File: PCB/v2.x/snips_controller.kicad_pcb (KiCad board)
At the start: 4 copper layers, 30 x 70 mm, 95 parts

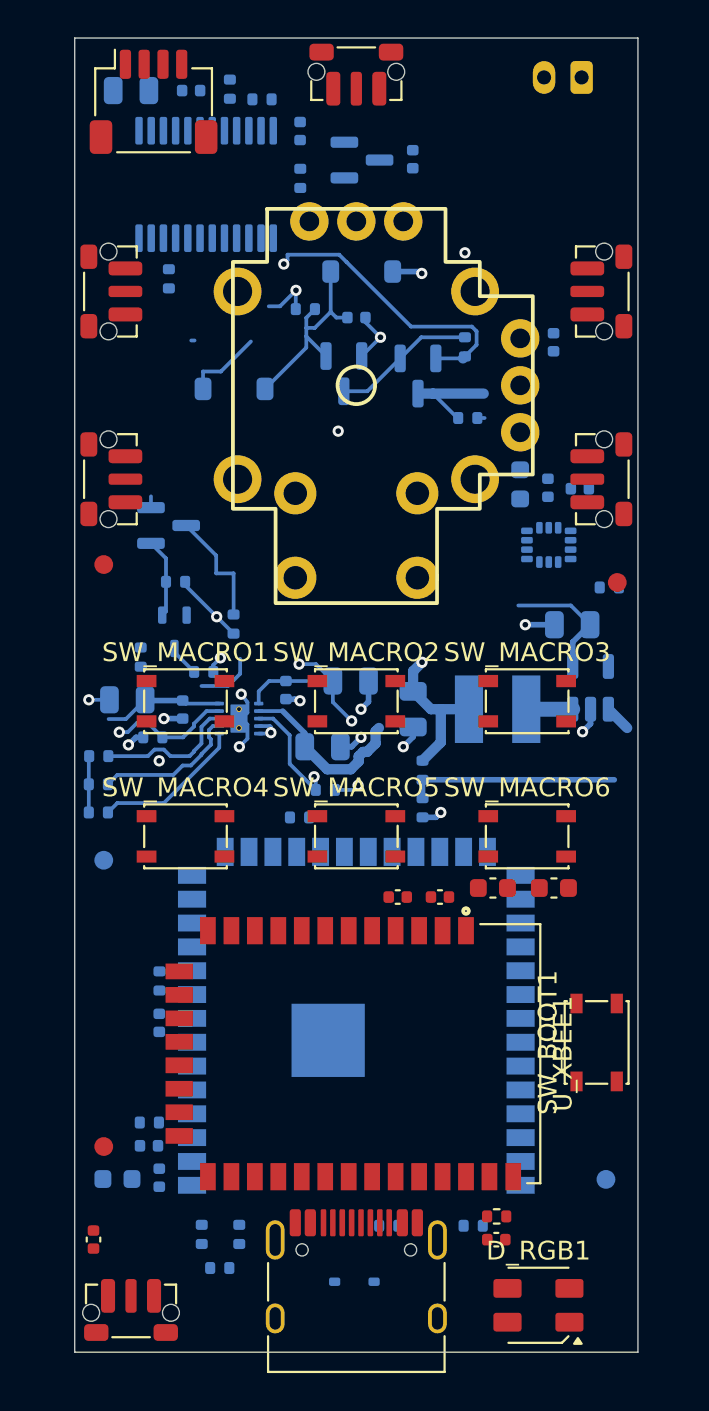
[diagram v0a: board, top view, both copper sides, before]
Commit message: Replace the V2 ESP32 and XBee with a BT840XE module (#97)
The XBee and ESP32 could not sit back to back: Espressif allows one
reflow and Digi forbids reflowing the XBee upside down. A single Fanstel
BT840XE (nRF52840 with PA) now runs the firmware and the Zigbee link.

The module sits on the bottom and reflows last, as Fanstel allows no
opposite-side reflow. The buck and charger moved to the top as rigid
blocks, with V1's copper. U_EXP1 is gone, since the module has enough
GPIOs for direct buttons.

Also from the pre-routing review:
- Hall sensor and stick on 3V3_RF, so they track the ADC reference
- RC filter on the trigger output
- 10 uF on the buck output, as the rail exceeded TI's 47 uF limit
- VBUS bypass at the module
- Tag-Connect SWD pads and a reset button
- Four M2 mounting holes
- Silkscreen reduced to labels a builder needs

Placed, not routed.

Co-authored-by: Claude Opus 5.5 <noreply@anthropic.com>
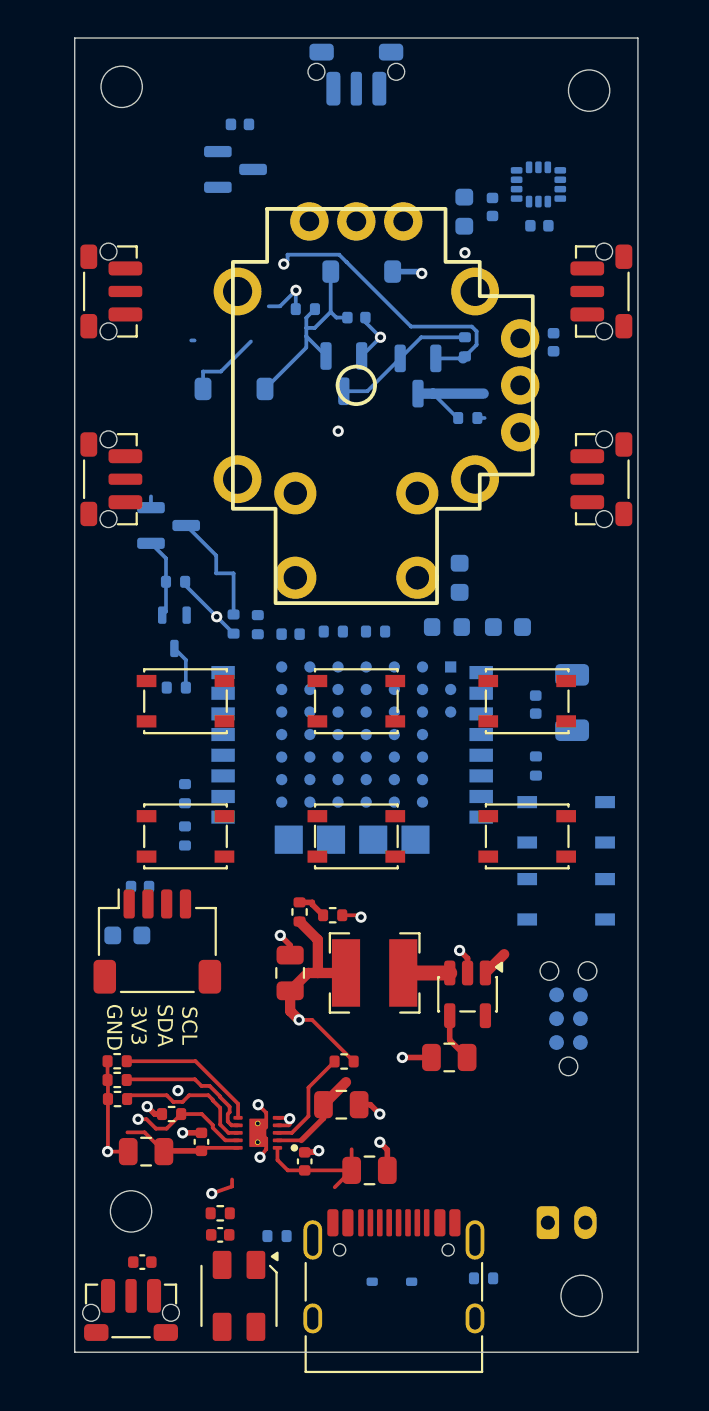
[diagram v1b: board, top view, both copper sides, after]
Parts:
- removed C_3V3_3: 39pF, Capacitor_SMD:C_0402_1005Metric
- removed C_EXP1: 100nF, C_0402_1005Metric
- removed C_XBEE_RC1, C_XBEE_VCC1: 100nF, Capacitor_SMD:C_0402_1005Metric
- removed C_XBEE_VCC2: 1µF, Capacitor_SMD:C_0603_1608Metric
- removed C_XBEE_VCC3: 47pF, Capacitor_SMD:C_0402_1005Metric
- removed C_XBEE_VCC4: 10µF, Capacitor_SMD:C_0603_1608Metric
- removed FID1, FID2, FID3, FID4, FID5: Fiducial_1mm_Mask2mm, Fiducial:Fiducial_1mm_Mask2mm
- removed R_EN_PU1, R_XBEE_ATTN_PU1, R_XBEE_RST1: 10kΩ, Resistor_SMD:R_0402_1005Metric
- removed R_EXP_INT1: 10kΩ, R_0402_1005Metric
- removed R_USB_DM1, R_USB_DP1: 27Ω, Resistor_SMD:R_0402_1005Metric
- removed R_XBEE_RC1: 100Ω, Resistor_SMD:R_0402_1005Metric
- removed U_EXP1: TCA9555PWR, TSSOP-24_4.4x7.8mm_P0.65mm
- removed U_XBEE1: XBee3 PRO Micro, XB3-24Z8UM
- added C_RF_BULK1: 47µF, C_1206_3216Metric, B.Cu at (146.5, 95.4)
- added C_TRIG1: 100nF, C_0402_1005Metric, B.Cu at (131.5, 91.8)
- added C_VBUS1: 1µF, C_0603_1608Metric, B.Cu at (140.5, 88.8)
- added FB_RF1: 600Ω@100MHz, L_0603_1608Metric, B.Cu at (139.8, 91.4)
- added J_SWD1: TC2030-NL, Tag-Connect_TC2030-IDC-NL_2x03_P1.27mm_Vertical, B.Cu at (146.3, 112.2)
- added MH1: MountingHole_2.2mm_M2_ISO14580, MountingHole:MountingHole_2.2mm_M2_ISO14580, F.Cu at (122.5, 62.6)
- added MH2: MountingHole_2.2mm_M2_ISO14580, MountingHole:MountingHole_2.2mm_M2_ISO14580, F.Cu at (147.4, 62.8)
- added MH3: MountingHole_2.2mm_M2_ISO14580, MountingHole:MountingHole_2.2mm_M2_ISO14580, F.Cu at (123.0, 122.5)
- added MH4: MountingHole_2.2mm_M2_ISO14580, MountingHole:MountingHole_2.2mm_M2_ISO14580, F.Cu at (147.0, 127.0)
- added R_TRIG1: 1kΩ, R_0402_1005Metric, B.Cu at (129.8, 91.2)
- added SW_RST1: SKRPABE010, SW_Alps_SKRP, B.Cu at (146.2, 101.8)
- C_BAT1, C_BUCK_IN1, C_SYS_1, C_SYS_2, C_VIN_1, C_VIN_2, L_BUCK1, R_FB1, R_FB2, R_ISET1, R_STAT1, R_STAT2, R_TS1, R_VSET1, U_BUCK1, U_CHG1: moved to F.Cu
- C_BUCK_OUT1: value 22µF -> 10µF; moved to F.Cu
- C_OLED_1: value 10µF -> 1µF; footprint Capacitor_SMD:C_0805_2012Metric -> C_0603_1608Metric
- SW_BOOT1, SW_TRIG_DIG1: moved to B.Cu
- U_MCU1: value ESP32-S3-WROOM-1U-N8 -> BT840XE; footprint ESP32-S3-WROOM-1U -> BT840XE
- moved BT1 61.0 mm to (145.2, 123.1), turned to 0 degrees
- moved C_OLED_1 45.0 mm to (122.8, 107.8), turned to 180 degrees
- moved U_OLED1 44.7 mm to (124.4, 108.1)
- moved C_OLED_2 42.5 mm to (123.5, 105.2), turned to 180 degrees
- moved R_I2C_SDA1 39.4 mm to (125.9, 102.5), turned to 90 degrees
- moved R_I2C_SCL1 37.6 mm to (125.9, 100.2)
- moved C_3V3_1 36.0 mm to (143.1, 91.4)
- moved C_3V3_2 32.2 mm to (144.6, 95.5)
- moved C_SYS_1 26.1 mm to (135.7, 120.3)
- moved C_SYS_2 25.1 mm to (132.2, 119.8), turned to 90 degrees
- moved C_VIN_1 24.1 mm to (123.8, 119.3)
- moved C_BUCK_IN1 24.0 mm to (139.9, 114.3)
- moved C_VIN_2 23.0 mm to (126.8, 118.8), turned to 90 degrees
- moved U_CHG1 22.1 mm to (129.8, 118.3)
- moved R_VSYS1 20.7 mm to (133.8, 91.6), turned to 0 degrees
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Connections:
- C_3V3_1 pad 1: 3V3 -> /MCU_Core/3V3_RF
- C_3V3_2 pad 1: 3V3 -> /MCU_Core/3V3_RF
- C_HALL1 pad 1: 3V3 -> /MCU_Core/3V3_RF
- C_STICK1 pad 1: 3V3 -> /MCU_Core/3V3_RF
- J_STICK1 pad 3: 3V3 -> /MCU_Core/3V3_RF
- J_STICK1 pad 3': 3V3 -> /MCU_Core/3V3_RF
- U_HALL1 pad 1: 3V3 -> /MCU_Core/3V3_RF
- U_MCU1 pad 1: GND -> /Accelerometer/I2C_SDA
- U_MCU1 pad 10: /Buttons_Direct/BTN_THR_DN -> GND
- U_MCU1 pad 11: /Buttons_Direct/BTN_INT -> /MCU_Core/PWR_BTN_SENSE
- U_MCU1 pad 12: /Accelerometer/I2C_SDA -> /MCU_Core/MCU_BOOT
- U_MCU1 pad 13: /MCU_Core/USB_DM_MCU -> /MCU_Core/RGB_DIN
- U_MCU1 pad 14: /MCU_Core/USB_DP_MCU -> /MCU_Core/MCU_RESET
- U_MCU1 pad 15: (no net) -> /MCU_Core/SWDCLK
- U_MCU1 pad 16: ACCEL_INT1 -> /MCU_Core/SWDIO
- U_MCU1 pad 2: 3V3 -> /Accelerometer/I2C_SCL
- U_MCU1 pad 3: /MCU_Core/MCU_EN -> (no net)
- U_MCU1 pad 4: /Hall_Trigger/TRIG_ANALOG -> (no net)
- U_MCU1 pad 7: /MCU_Core/VSYS_SENSE -> (no net)
- U_MCU1 pad 8: /XBee/XBEE_SPI_ATTN -> (no net)
- U_MCU1 pad 9: /Buttons_Direct/BTN_THR_UP -> /MCU_Core/3V3_RF
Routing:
- net /Power_Buck/BUCK_FB: track 11.2 -> 1.60 mm
- net VSYS: track 36.2 -> 29.6 mm, vias 4 -> 2
- net VBAT: track 9.56 -> 5.36 mm
- net 3V3: track 11.5 -> 14.6 mm, vias 4 -> 3
- net /MCU_Core/PWR_BTN_SENSE: track 4.83 -> 2.54 mm
- net GND: track 26.0 -> 27.8 mm
- net /MCU_Core/STAT2: track 6.25 -> 5.51 mm, vias 1 -> 0
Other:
- board text added: "+"
- board text added: "-"
- board text added: "3V3"
- board text added: "BOOT"
- board text added: "GND"
- board text added: "RESET"
- board text added: "SCL"
- board text added: "SDA"

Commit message: Route the V2 board and add production files
Fully routed on four layers: In2 is a solid ground plane, and In1 carries
signals with a partial 3V3 fill. BUCK_FB stays on the top layer and out
from under the inductor. Every GND pad has a via to the plane.

BTN_MACRO4 moved from P0.21 (E2) to P1.11 (Z0), since E2 had no escape
and Z0 sits beside the button.

Adds six fiducials, the Snips logo at 80%, a lower-density QR code that
prints at 5.5 mm, and the V2.0 text. Production files follow V1's layout.

Co-Authored-By: Claude Opus 5.5 <noreply@anthropic.com>
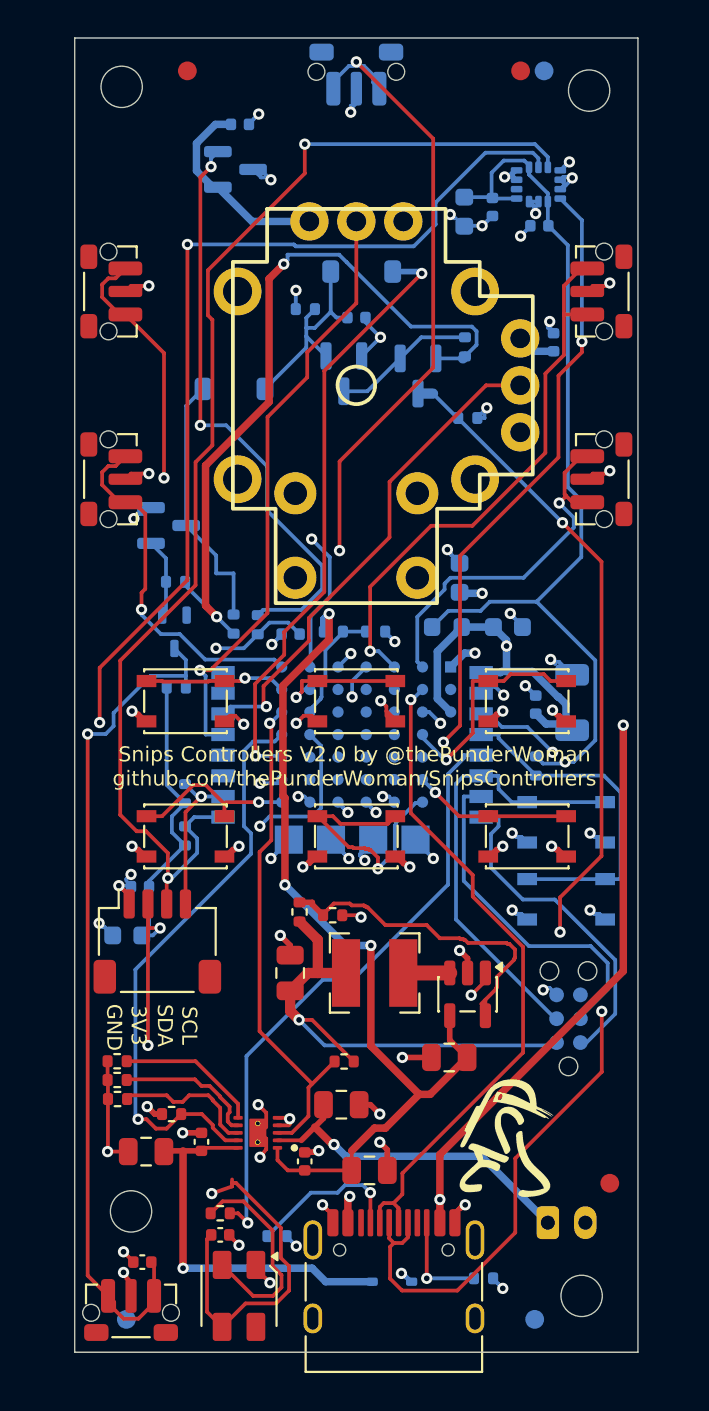
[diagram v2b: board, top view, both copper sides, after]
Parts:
- added FID1: Fiducial_1mm_Mask2mm, Fiducial:Fiducial_1mm_Mask2mm, F.Cu at (126.0, 61.8)
- added FID2: Fiducial_1mm_Mask2mm, Fiducial:Fiducial_1mm_Mask2mm, F.Cu at (143.8, 61.8)
- added FID3: Fiducial_1mm_Mask2mm, Fiducial:Fiducial_1mm_Mask2mm, F.Cu at (148.5, 121.0)
- added FID4: Fiducial_1mm_Mask2mm, Fiducial:Fiducial_1mm_Mask2mm, B.Cu at (145.0, 61.8)
- added FID5: Fiducial_1mm_Mask2mm, Fiducial:Fiducial_1mm_Mask2mm, B.Cu at (122.8, 128.2)
- added FID6: Fiducial_1mm_Mask2mm, Fiducial:Fiducial_1mm_Mask2mm, B.Cu at (144.5, 128.2)
- LOGO3: moved to F.Cu
- moved LOGO2 65.7 mm to (123.1, 115.0)
- moved LOGO3 63.9 mm to (143.0, 118.6), turned to 0 degrees
- moved LOGO1 32.8 mm to (123.2, 67.2), turned to 0 degrees
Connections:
- U_MCU1 pad E2: /Buttons_Direct/BTN_MACRO4 -> (no net)
- U_MCU1 pad Z0: (no net) -> /Buttons_Direct/BTN_MACRO4
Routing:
- net 3V3: track 14.6 -> 163.9 mm, vias 3 -> 6
- net VBUS: track 6.40 -> 85.7 mm, vias 0 -> 6
- net /MCU_Core/PWR_BTN_SENSE: track 2.54 -> 79.3 mm, vias 0 -> 2
- net GND: track 27.8 -> 95.0 mm, vias 16 -> 75
- net /Accelerometer/I2C_SDA: track 0.00 -> 65.9 mm, vias 0 -> 2
- net VSYS: track 29.6 -> 94.8 mm, vias 2 -> 5
- net /Accelerometer/I2C_SCL: track 0.00 -> 64.9 mm, vias 0 -> 3
- net /MCU_Core/3V3_RF: track 0.00 -> 62.9 mm, vias 0 -> 1
- net /MCU_Core/USB_DP: track 0.00 -> 50.3 mm, vias 0 -> 2
- net ACCEL_INT1: track 0.00 -> 44.4 mm, vias 0 -> 3
- net /Buttons_Direct/BTN_TRIG_DIG: track 0.00 -> 43.9 mm, vias 0 -> 3
- net /MCU_Core/USB_DM: track 0.00 -> 35.8 mm, vias 0 -> 1
- net /Power_Buck/PWR_EN: track 6.79 -> 41.8 mm, vias 1 -> 3
- net /MCU_Core/RGB_DIN: track 0.00 -> 32.8 mm, vias 0 -> 1
- net /MCU_Core/STICK_X: track 0.00 -> 32.2 mm, vias 0 -> 1
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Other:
- board text added: "Snips Controllers V2.0 by @thePunderWoman github.com/thePunderWoman/SnipsControllers"

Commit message: V2 PCB: ESP32-S3-MINI-1U with an optional castellated XBee carrier
Replace the BT840XE with an ESP32-S3-MINI-1U-N8 on the top side, and move
the XBee to an optional hand-soldered daughter board on the underside,
linked by UART with flow control instead of SPI. The WROOM-1U does not fit
between the macro row and USB; the MINI-1U does.

Turn the module 270 degrees and assign pins by position, so the signal
pins face the stick, OLED and carrier. PWR_HOLD stays on RXD0, whose
reset pull-up holds the latch, and IO26 stays unconnected because
Arduino's PSRAM probe drives it at every boot.

Put the buck and charger back on the bottom, remove the reset button and
SWD footprint, move the hall sensor away from the stick, reroute the
board, and regenerate the production files.

Co-Authored-By: Claude Opus 5.5 <noreply@anthropic.com>
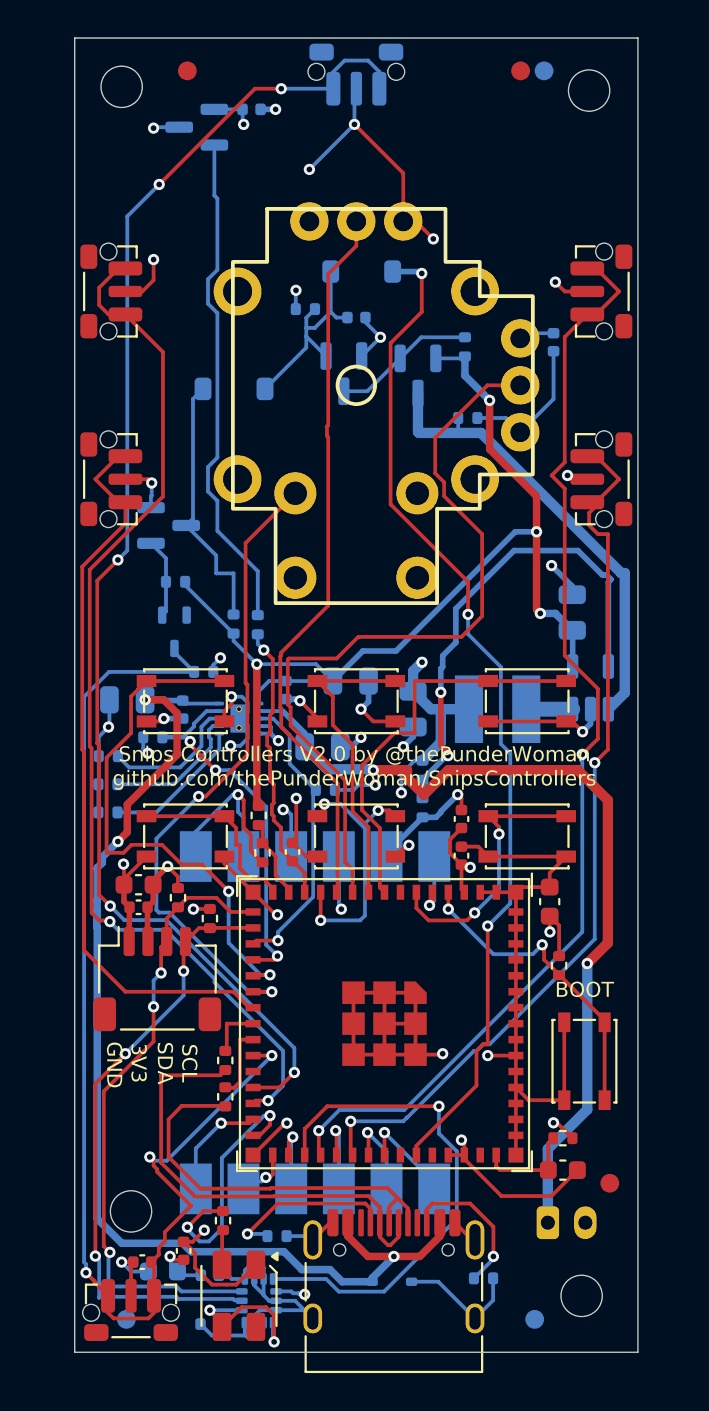
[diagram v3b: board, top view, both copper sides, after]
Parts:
- removed C_RF_BULK1: 47µF, C_1206_3216Metric
- removed C_VBUS1: 1µF, C_0603_1608Metric
- removed FB_RF1: 600Ω@100MHz, L_0603_1608Metric
- removed J_SWD1: TC2030-NL, Tag-Connect_TC2030-IDC-NL_2x03_P1.27mm_Vertical
- removed SW_RST1: SKRPABE010, SW_Alps_SKRP
- added C_3V3_3: 39pF, C_0402_1005Metric, F.Cu at (140.6, 103.5)
- added C_EN1: 1µF, C_0603_1608Metric, F.Cu at (146.0, 120.3)
- added R_EN_PU1: 10kΩ, R_0402_1005Metric, F.Cu at (146.0, 118.6)
- added R_USB_DM1: 27Ω, R_0402_1005Metric, F.Cu at (128.0, 114.5)
- added R_USB_DP1: 27Ω, R_0402_1005Metric, F.Cu at (128.0, 116.4)
- added U_XBEE1: XBee carrier, XBee_Carrier_Castellated, B.Cu at (131.5, 112.5)
- C_3V3_1, C_3V3_2, C_OLED_1, C_OLED_2, C_TRIG1, R_BOOT_PU1, R_I2C_SCL1, R_I2C_SDA1, R_VSYS1, R_VSYS2, SW_BOOT1: moved to F.Cu
- C_BAT1, C_BUCK_IN1, C_SYS_1, C_SYS_2, C_VIN_1, C_VIN_2, LOGO3, L_BUCK1, R_FB1, R_FB2, R_ISET1, R_STAT1, R_STAT2, R_TS1, R_VSET1, U_BUCK1, U_CHG1: moved to B.Cu
- C_BUCK_OUT1: value 10µF -> 22µF; moved to B.Cu
- U_MCU1: value BT840XE -> ESP32-S3-MINI-1U-N8; footprint BT840XE -> ESP32-S3-MINI-1U; moved to F.Cu
- moved U_IMU1 61.3 mm to (129.8, 127.3), turned to -90 degrees
- moved C_IMU_3 61.1 mm to (127.2, 128.5)
- moved C_IMU_1 58.9 mm to (127.2, 125.9), turned to 0 degrees
- moved C_IMU_2 58.7 mm to (124.7, 125.7), turned to 180 degrees
- moved LOGO1 44.0 mm to (130.6, 110.6)
- moved C_SYS_1 26.1 mm to (134.7, 94.2)
- moved C_SYS_2 25.1 mm to (131.2, 94.7), turned to -90 degrees
- moved C_BUCK_IN1 24.6 mm to (146.5, 90.6), turned to 90 degrees
- moved C_VIN_1 24.1 mm to (122.8, 95.2)
- moved LOGO2 24.1 mm to (146.2, 108.2)
- moved C_VIN_2 23.0 mm to (125.8, 95.8), turned to -90 degrees
- moved U_CHG1 22.1 mm to (128.8, 96.2)
- moved R_STAT1 20.1 mm to (124.2, 97.2)
- moved C_BAT1 19.1 mm to (133.2, 97.8)
- moved R_ISET1 18.3 mm to (121.8, 98.2)
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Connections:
- C_3V3_1 pad 1: /MCU_Core/3V3_RF -> 3V3
- C_3V3_2 pad 1: /MCU_Core/3V3_RF -> 3V3
- C_HALL1 pad 1: /MCU_Core/3V3_RF -> 3V3
- C_STICK1 pad 1: /MCU_Core/3V3_RF -> 3V3
- J_STICK1 pad 3: /MCU_Core/3V3_RF -> 3V3
- J_STICK1 pad 3': /MCU_Core/3V3_RF -> 3V3
- U_HALL1 pad 1: /MCU_Core/3V3_RF -> 3V3
- U_MCU1 pad 1: /Accelerometer/I2C_SDA -> GND
- U_MCU1 pad 10: GND -> /MCU_Core/STICK_Y
- U_MCU1 pad 11: /MCU_Core/PWR_BTN_SENSE -> /MCU_Core/STICK_X
- U_MCU1 pad 12: /MCU_Core/MCU_BOOT -> /Buttons_Direct/BTN_MACRO5
- U_MCU1 pad 13: /MCU_Core/RGB_DIN -> /Hall_Trigger/TRIG_ADC
- U_MCU1 pad 14: /MCU_Core/MCU_RESET -> /MCU_Core/VSYS_SENSE
- U_MCU1 pad 15: /MCU_Core/SWDCLK -> /Buttons_Direct/BTN_MACRO4
- U_MCU1 pad 16: /MCU_Core/SWDIO -> /Accelerometer/I2C_SDA
- U_MCU1 pad 2: /Accelerometer/I2C_SCL -> GND
- U_MCU1 pad 3: (no net) -> 3V3
- U_MCU1 pad 4: (no net) -> /MCU_Core/MCU_BOOT
- U_MCU1 pad 5: /MCU_Core/STICK_X -> /XBee/XBEE_SLEEP_RQ
- U_MCU1 pad 6: /MCU_Core/STICK_Y -> /Buttons_Direct/BTN_MACRO6
- U_MCU1 pad 8: (no net) -> /Buttons_Direct/BTN_MACRO3
- U_MCU1 pad 9: /MCU_Core/3V3_RF -> /Buttons_Direct/BTN_MACRO2
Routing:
- net GND: track 95.0 -> 208.0 mm, vias 75 -> 34
- net 3V3: track 163.9 -> 53.7 mm, vias 6 -> 17
- net /MCU_Core/3V3_RF: track 62.9 -> 0.00 mm, vias 1 -> 0
- net VSYS: track 94.8 -> 57.9 mm, vias 5 -> 4
- net /Accelerometer/I2C_SCL: track 64.9 -> 32.7 mm
- net /Accelerometer/I2C_SDA: track 65.9 -> 33.7 mm, vias 2 -> 3
- net /Buttons_Direct/BTN_VOL_UP: track 29.5 -> 59.2 mm, vias 1 -> 2
- net /Buttons_Direct/BTN_TRIG_DIG: track 43.9 -> 73.0 mm, vias 3 -> 5
- net /MCU_Core/USB_DP: track 50.3 -> 21.6 mm, vias 2 -> 0
- net /Buttons_Direct/BTN_VOL_DN: track 19.5 -> 47.8 mm, vias 1 -> 2
- net VBAT: track 18.2 -> 46.1 mm, vias 1 -> 2
- net VBUS: track 85.7 -> 59.8 mm, vias 6 -> 3
- net /Buttons_Direct/BTN_THR_UP: track 30.3 -> 55.9 mm
- net /MCU_Core/MCU_RESET: track 23.9 -> 0.00 mm
- net /MCU_Core/BTN_STICK: track 10.9 -> 34.5 mm, vias 1 -> 2
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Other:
- board text removed: "RESET"
